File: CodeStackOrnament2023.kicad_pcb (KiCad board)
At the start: 2 copper layers, 70 x 70 mm, 28 parts, among them SW1 SW_SPST, U1 TLC555xD, U2 74VHC4040FT

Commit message: silkscreen logos
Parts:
- added G***: LOGO, LOGO, B.Cu at (131.8, 121.6)
- added G***: LOGO, LOGO, B.Cu at (173.7, 103.7)
- added G***: LOGO, LOGO, B.Cu at (129.1, 103.0)

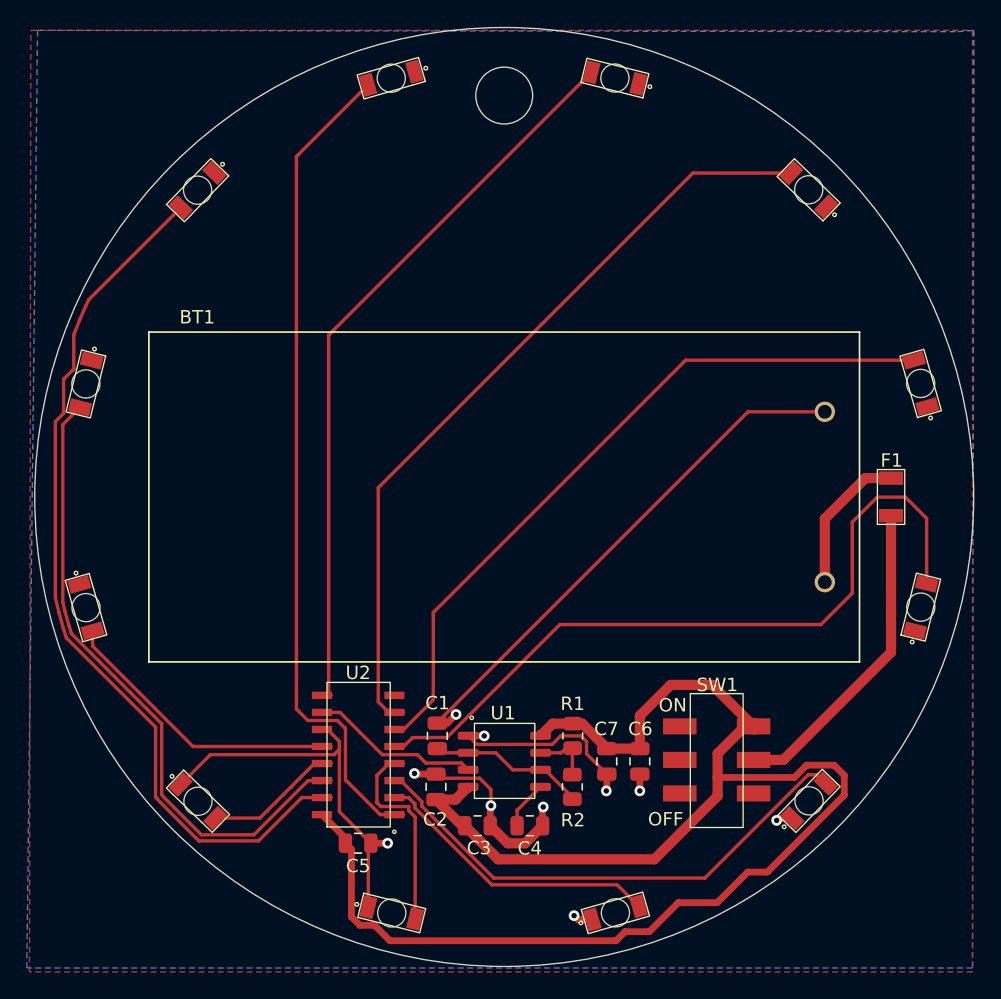
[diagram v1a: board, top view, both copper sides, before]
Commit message: adding qr code and a few more logos for silkscreen.
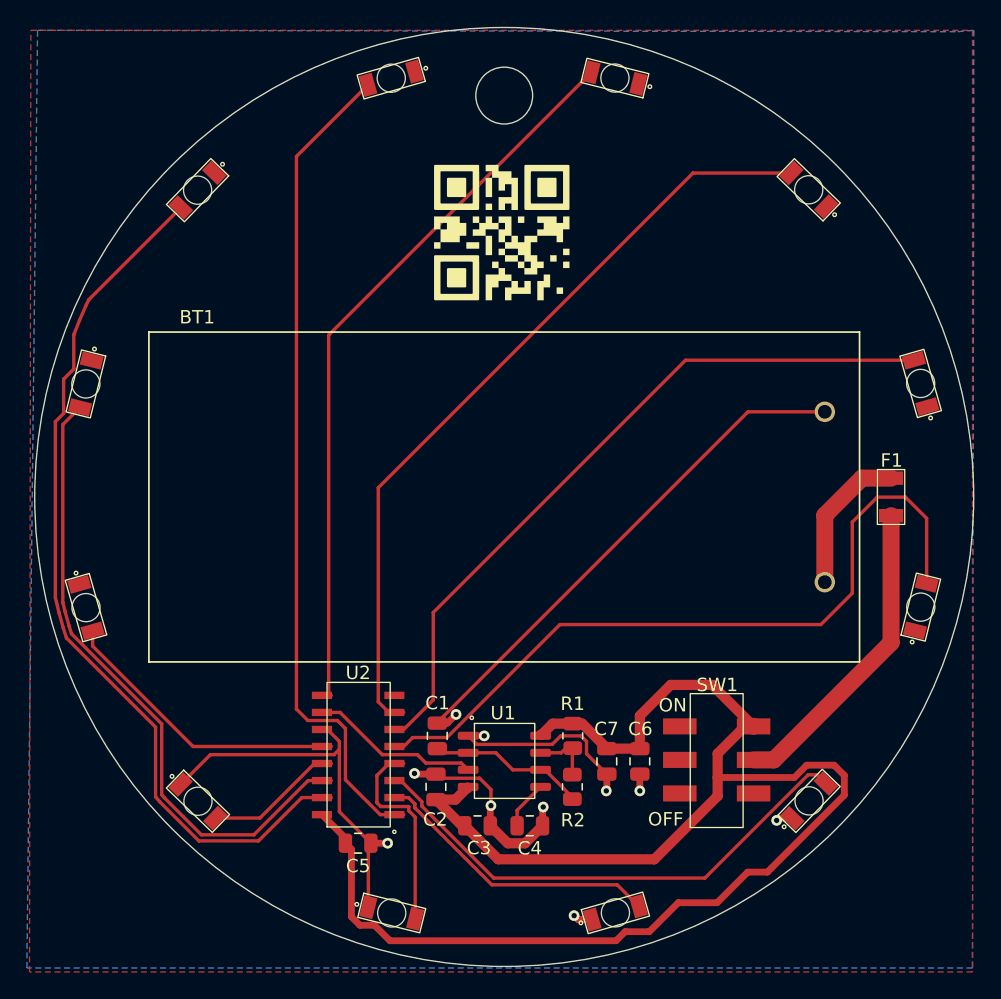
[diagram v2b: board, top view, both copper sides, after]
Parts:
- added G***: LOGO, LOGO, F.Cu at (149.9, 85.0)
- added G***: LOGO, LOGO, B.Cu at (127.3, 90.4)
- added G***: LOGO, LOGO, B.Cu at (171.6, 89.7)
- added G***: LOGO, LOGO, B.Cu at (171.6, 120.7)
- moved G*** 4.54 mm to (124.8, 104.5)
- moved G*** 2.16 mm to (150.1, 82.0)
- moved G*** 1.59 mm to (175.3, 103.7)
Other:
- board text added: "[1024]"
- board text added: "[128]"
- board text added: "[16]"
- board text added: "[1]"
- board text added: "[2048]"
- board text added: "[256]"
- board text added: "[2]"
- board text added: "[32]"
- board text added: "[4]"
- board text added: "[512]"
- board text added: "[64]"
- board text added: "[8]"

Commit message: fixing drc
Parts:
- moved G*** 0.55 mm to (149.8, 85.5)
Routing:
- net GND: track 103.8 -> 65.3 mm
- net Net-(D11-A): track 66.3 -> 66.9 mm
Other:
- board text added: "FROM: JON"
- board text added: "MERRY CHRISTMAS!"
- board text added: "SCAN FOR INSTRUCTIONS ->"
- board text added: "TO: ______________"

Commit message: fixing last drc
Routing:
- net GND: track 65.3 -> 20.1 mm

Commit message: aligning silkscreen
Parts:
- moved G*** 30.3 mm to (126.8, 91.8)
- moved G*** 27.2 mm to (126.8, 117.5)
- moved G*** 3.47 mm to (173.0, 117.5)
- moved G*** 2.46 mm to (173.0, 91.8)
- moved G*** 1.12 mm to (175.8, 104.7)
- moved G*** 0.78 mm to (150.2, 82.8)
- moved G*** 0.52 mm to (124.3, 104.7)
- moved G*** 0.17 mm to (150.2, 126.7)

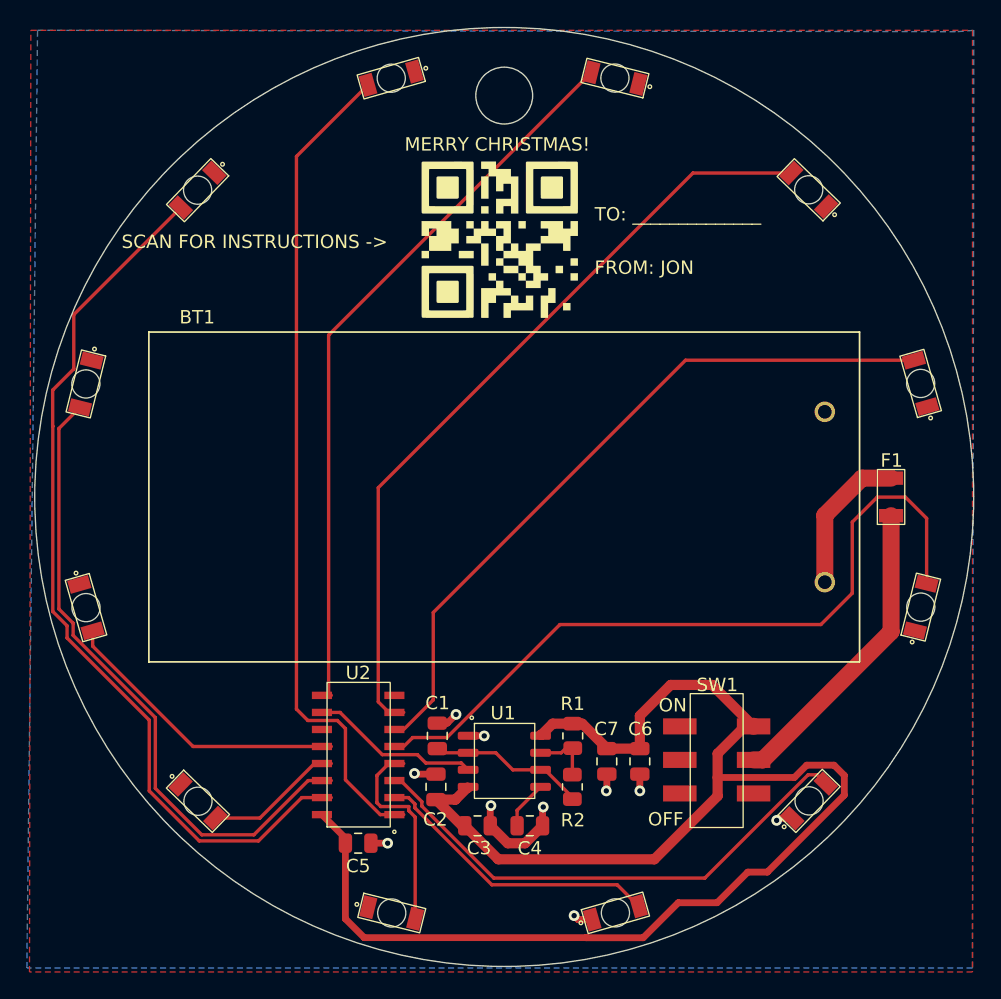
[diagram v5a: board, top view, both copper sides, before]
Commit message: more alignment with u2
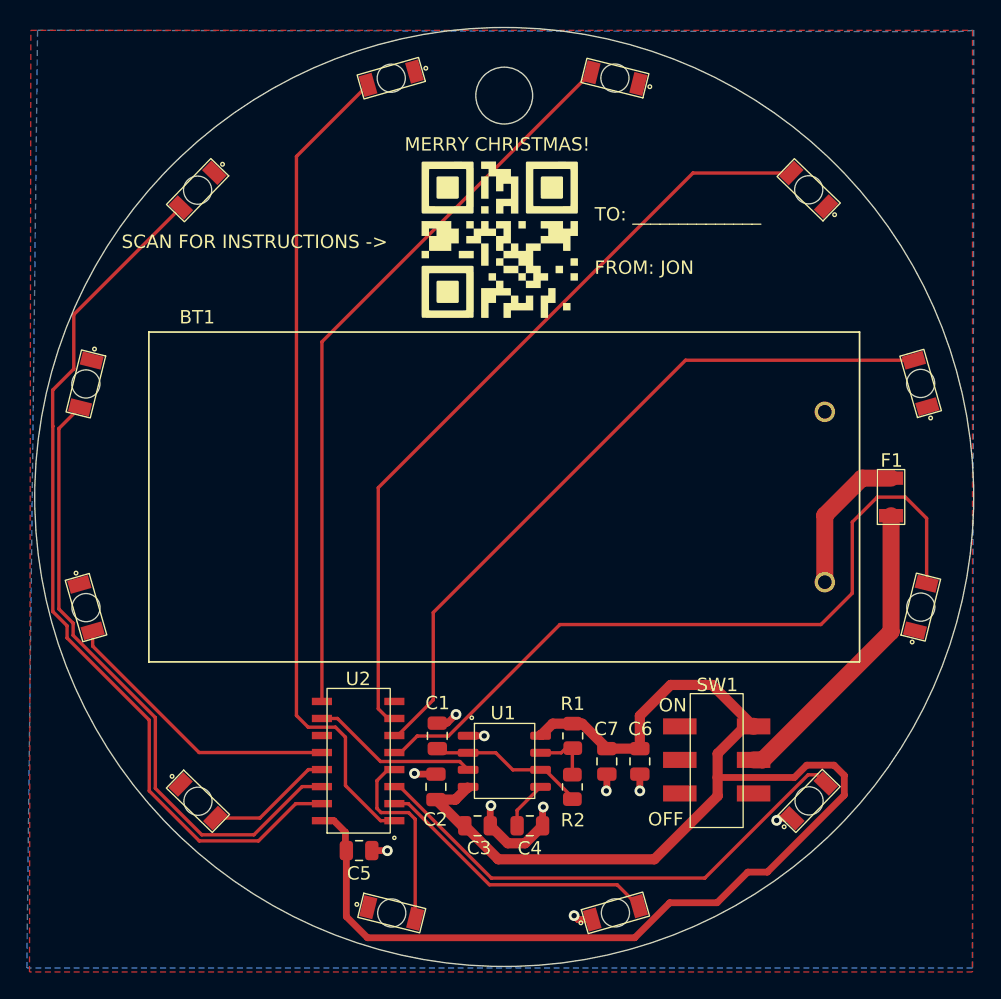
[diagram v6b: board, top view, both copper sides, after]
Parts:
- moved C5 0.55 mm to (139.3, 131.1)
- moved U2 0.45 mm to (141.9, 128.8)
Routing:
- net Net-(D7-A): track 15.5 -> 14.3 mm
- net Net-(D10-A): track 48.3 -> 47.4 mm
- net Net-(D3-A): track 53.3 -> 54.1 mm
- net Net-(D4-A): track 55.3 -> 56.2 mm
- net Net-(D8-A): track 10.3 -> 9.44 mm
- net Net-(D11-A): track 66.9 -> 66.0 mm
- net GND: track 20.1 -> 19.3 mm
- net Net-(D1-A): track 54.7 -> 55.2 mm
- net Net-(D9-A): track 22.0 -> 21.5 mm
- net Net-(U1-Q): track 12.0 -> 12.5 mm

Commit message: adding gerbers
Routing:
- net Net-(D2-A): track 58.5 -> 54.2 mm
- net Net-(D3-A): track 54.1 -> 50.3 mm
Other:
- board text added: "JLCJLCJLCJLC"
- board text added: "SCAN FOR DETAILS ->"
- board text removed: "SCAN FOR INSTRUCTIONS ->"
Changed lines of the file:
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@@
     (effects (font (size 1 1) (thickness 0.15)) (justify left bottom))
   )
-  (gr_text "SCAN FOR INSTRUCTIONS ->" (at 121.56 86.25) (layer "F.SilkS")
+  (gr_text "JLCJLCJLCJLC" (at 145.32 105.34) (layer "F.SilkS")
+    (effects (font (size 1 1) (thickness 0.15)) (justify left bottom))
+  )
+  (gr_text "SCAN FOR DETAILS ->" (at 125.78 86.32) (layer "F.SilkS")
     (effects (font (size 1 1) (thickness 0.15)) (justify left bottom))
   )
@@
   (segment (start 152.8 126.3) (end 151.05 128.05) (width 0.254) (layer "F.Cu") (net 5))
   (segment (start 151.05 128.05) (end 151.05 129.2) (width 0.254) (layer "F.Cu") (net 5))
-  (segment (start 136.5 119.931152) (end 136.5 93.119964) (width 0.254) (layer "F.Cu") (net 6))
-  (segment (start 136.5 93.119964) (end 156.596492 73.023472) (width 0.254) (layer "F.Cu") (net 6))
+  (segment (start 156.596492 73.193508) (end 156.596492 73.023472) (width 0.254) (layer "F.Cu") (net 6))
+  (segment (start 136.5 119.931152) (end 136.5 93.29) (width 0.254) (layer "F.Cu") (net 6))
+  (segment (start 136.5 93.29) (end 156.596492 73.193508) (width 0.254) (layer "F.Cu") (net 6))
+  (segment (start 171.482449 80.537551) (end 140.7 111.32) (width 0.254) (layer "F.Cu") (net 7))
+  (segment (start 140.7 111.32) (end 140.7 120.476152) (width 0.254) (layer "F.Cu") (net 7))
   (segment (start 140.7 120.476152) (end 141.425 121.201152) (width 0.254) (layer "F.Cu") (net 7))
-  (segment (start 140.7 104) (end 140.7 120.476152) (width 0.254) (layer "F.Cu") (net 7))
-  (segment (start 171.494652 80.537551) (end 164.162449 80.537551) (width 0.254) (layer "F.Cu") (net 7))
   (segment (start 141.425 121.201152) (end 141.9 121.201152) (width 0.254) (layer "F.Cu") (net 7))
-  (segment (start 164.162449 80.537551) (end 140.7 104) (width 0.254) (layer "F.Cu") (net 7))
-  (segment (start 144.8 119.82) (end 142.148848 122.471152) (width 0.254) (layer "F.Cu") (net 8))
-  (segment (start 142.148848 122.471152) (end 141.9 122.471152) (width 0.254) (layer "F.Cu") (net 8))
-  (segment (start 144.8 119.82) (end 144.8 113.3) (width 0.254) (layer "F.Cu") (net 8))
-  (segment (start 144.8 113.3) (end 163.605984 94.494016) (width 0.254) (layer "F.Cu") (net 8))
-  (segment (start 163.605984 94.494016) (end 180.6398 94.494016) (width 0.254) (layer "F.Cu") (net 8))
+  (segment (start 171.494652 80.537551) (end 171.482449 80.537551) (width 0.254) (layer "F.Cu") (net 7))
+  (segment (start 141.9 122.471152) (end 142.478848 122.471152) (width 0.254) (layer "F.Cu") (net 8))
+  (segment (start 142.478848 122.471152) (end 170.455984 94.494016) (width 0.254) (layer "F.Cu") (net 8))
+  (segment (start 170.455984 94.494016) (end 180.6398 94.494016) (width 0.254) (layer "F.Cu") (net 8))
   (segment (start 176.038 106.562) (end 176.038 111.862) (width 0.254) (layer "F.Cu") (net 9))
   (segment (start 177.9 104.7) (end 176.038 106.562) (width 0.254) (layer "F.Cu") (net 9))
@@
   (segment (start 119.408419 115.808419) (end 127.341152 123.741152) (width 0.254) (layer "F.Cu") (net 14))
   (segment (start 119.408419 114.667703) (end 119.408419 115.808419) (width 0.254) (layer "F.Cu") (net 14))
-  (segment (start 131.426034 129.873966) (end 127.545282 129.873966) (width 0.254) (layer "F.Cu") (net 15))
+  (segment (start 116.9 113.157948) (end 116.9 99.5752) (width 0.254) (layer "F.Cu") (net 15))
+  (segment (start 124.08 121.134065) (end 118.174 115.228065) (width 0.254) (layer "F.Cu") (net 15))
+  (segment (start 116.9 99.5752) (end 118.466724 98.008476) (width 0.254) (layer "F.Cu") (net 15))
+  (segment (start 136.025 126.281152) (end 132.432186 129.873966) (width 0.254) (layer "F.Cu") (net 15))
   (segment (start 127.545282 129.873966) (end 124.08 126.408684) (width 0.254) (layer "F.Cu") (net 15))
-  (segment (start 135.018848 126.281152) (end 136.5 126.281152) (width 0.254) (layer "F.Cu") (net 15))
-  (segment (start 116.89 113.037948) (end 116.89 99.5852) (width 0.254) (layer "F.Cu") (net 15))
-  (segment (start 124.08 121.134064) (end 117.954 115.008064) (width 0.254) (layer "F.Cu") (net 15))
-  (segment (start 117.954 115.008064) (end 117.954 114.101948) (width 0.254) (layer "F.Cu") (net 15))
-  (segment (start 117.954 114.101948) (end 116.89 113.037948) (width 0.254) (layer "F.Cu") (net 15))
-  (segment (start 116.89 99.5852) (end 118.466724 98.008476) (width 0.254) (layer "F.Cu") (net 15))
-  (segment (start 124.08 126.408684) (end 124.08 121.134064) (width 0.254) (layer "F.Cu") (net 15))
-  (segment (start 131.426034 129.873966) (end 135.018848 126.281152) (width 0.254) (layer "F.Cu") (net 15))
-  (segment (start 117.5 114.29) (end 116.436 113.226) (width 0.254) (layer "F.Cu") (net 16))
-  (segment (start 123.626 126.596736) (end 123.626 121.322116) (width 0.254) (layer "F.Cu") (net 16))
-  (segment (start 116.426 96.720044) (end 118 95.146044) (width 0.254) (layer "F.Cu") (net 16))
-  (segment (start 116.436 99.417147) (end 116.426 99.407147) (width 0.254) (layer "F.Cu") (net 16))
-  (segment (start 117.5 115.196116) (end 117.5 114.29) (width 0.254) (layer "F.Cu") (net 16))
-  (segment (start 131.772034 130.327966) (end 134.548848 127.551152) (width 0.254) (layer "F.Cu") (net 16))
-  (segment (start 118 91.091119) (end 125.980803 83.110316) (width 0.254) (layer "F.Cu") (net 16))
-  (segment (start 131.772034 130.327966) (end 127.35723 130.327966) (width 0.254) (layer "F.Cu") (net 16))
-  (segment (start 118 95.146044) (end 118 91.091119) (width 0.254) (layer "F.Cu") (net 16))
-  (segment (start 116.426 99.407147) (end 116.426 96.720044) (width 0.254) (layer "F.Cu") (net 16))
+  (segment (start 118.174 115.228065) (end 118.174 114.431948) (width 0.254) (layer "F.Cu") (net 15))
+  (segment (start 124.08 126.408684) (end 124.08 121.134065) (width 0.254) (layer "F.Cu") (net 15))
+  (segment (start 118.174 114.431948) (end 116.9 113.157948) (width 0.254) (layer "F.Cu") (net 15))
+  (segment (start 136.5 126.281152) (end 136.025 126.281152) (width 0.254) (layer "F.Cu") (net 15))
+  (segment (start 132.432186 129.873966) (end 127.545282 129.873966) (width 0.254) (layer "F.Cu") (net 15))
+  (segment (start 117.31 94.5) (end 125.980803 85.829197) (width 0.254) (layer "F.Cu") (net 16))
+  (segment (start 133.248186 130.327966) (end 127.35723 130.327966) (width 0.254) (layer "F.Cu") (net 16))
+  (segment (start 116.446 113.346) (end 116.446 97.204) (width 0.254) (layer "F.Cu") (net 16))
+  (segment (start 136.025 127.551152) (end 133.248186 130.327966) (width 0.254) (layer "F.Cu") (net 16))
+  (segment (start 125.980803 85.829197) (end 125.980803 83.110316) (width 0.254) (layer "F.Cu") (net 16))
+  (segment (start 117.31 96.34) (end 117.31 94.5) (width 0.254) (layer "F.Cu") (net 16))
+  (segment (start 117.72 114.62) (end 116.446 113.346) (width 0.254) (layer "F.Cu") (net 16))
+  (segment (start 117.72 115.416117) (end 117.72 114.62) (width 0.254) (layer "F.Cu") (net 16))
   (segment (start 127.35723 130.327966) (end 123.626 126.596736) (width 0.254) (layer "F.Cu") (net 16))
-  (segment (start 134.548848 127.551152) (end 136.5 127.551152) (width 0.254) (layer "F.Cu") (net 16))
-  (segment (start 116.436 113.226) (end 116.436 99.417147) (width 0.254) (layer "F.Cu") (net 16))
-  (segment (start 123.626 121.322116) (end 117.5 115.196116) (width 0.254) (layer "F.Cu") (net 16))
-  (segment (start 137.51 121.85) (end 138.254 122.594) (width 0.254) (layer "F.Cu") (net 17))
+  (segment (start 136.5 127.551152) (end 136.025 127.551152) (width 0.254) (layer "F.Cu") (net 16))
+  (segment (start 123.626 121.322117) (end 117.72 115.416117) (width 0.254) (layer "F.Cu") (net 16))
+  (segment (start 116.446 97.204) (end 117.31 96.34) (width 0.254) (layer "F.Cu") (net 16))
+  (segment (start 123.626 126.596736) (end 123.626 121.322117) (width 0.254) (layer "F.Cu") (net 16))
+  (segment (start 139.937266 73.965171) (end 134.6 79.302437) (width 0.254) (layer "F.Cu") (net 17))
   (segment (start 134.6 79.302437) (end 134.6 120.980152) (width 0.254) (layer "F.Cu") (net 17))
+  (segment (start 140.05 128) (end 140.871152 128.821152) (width 0.254) (layer "F.Cu") (net 17))
   (segment (start 135.469848 121.85) (end 137.51 121.85) (width 0.254) (layer "F.Cu") (net 17))
-  (segment (start 139.937266 73.965171) (end 134.6 79.302437) (width 0.254) (layer "F.Cu") (net 17))
-  (segment (start 138.254 122.594) (end 138.254 126.204) (width 0.254) (layer "F.Cu") (net 17))
-  (segment (start 138.254 126.204) (end 140.871152 128.821152) (width 0.254) (layer "F.Cu") (net 17))
+  (segment (start 137.51 121.85) (end 140.05 124.39) (width 0.254) (layer "F.Cu") (net 17))
   (segment (start 140.871152 128.821152) (end 141.9 128.821152) (width 0.254) (layer "F.Cu") (net 17))
   (segment (start 134.6 120.980152) (end 135.469848 121.85) (width 0.254) (layer "F.Cu") (net 17))
+  (segment (start 140.05 124.39) (end 140.05 128) (width 0.254) (layer "F.Cu") (net 17))
   (segment (start 154.6875 123.4125) (end 154.34 123.76) (width 0.254) (layer "F.Cu") (net 18))
   (segment (start 155.2 123.4125) (end 154.6875 123.4125) (width 0.254) (layer "F.Cu") (net 18))

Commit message: adding gerbers. cleaning up schematic.
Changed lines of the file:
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@@
       (plotinvisibletext false)
       (sketchpadsonfab false)
-      (subtractmaskfromsilk false)
+      (subtractmaskfromsilk true)
       (outputformat 1)
       (mirror false)
-      (drillshape 1)
+      (drillshape 0)
       (scaleselection 1)
-      (outputdirectory "")
+      (outputdirectory "Gerbers/")
     )
   )
@@
     (fp_line (start 1 0.625) (end -1 0.625)
       (stroke (width 0.1) (type solid)) (layer "F.Fab"))
-    (pad "1" smd roundrect (at -0.9125 0 270) (size 1.025 1.4) (layers "F.Cu" "F.Paste" "F.Mask") (roundrect_rratio 0.243902)
+    (pad "1" smd roundrect (at -0.9125 0 270) (size 1.025 1.4) (layers "F.Cu" "F.Paste" "F.Mask") (roundrect_rratio 0.243902439)
       (net 18 "Net-(U1-DIS)") (pintype "passive"))
-    (pad "2" smd roundrect (at 0.9125 0 270) (size 1.025 1.4) (layers "F.Cu" "F.Paste" "F.Mask") (roundrect_rratio 0.243902)
+    (pad "2" smd roundrect (at 0.9125 0 270) (size 1.025 1.4) (layers "F.Cu" "F.Paste" "F.Mask") (roundrect_rratio 0.243902439)
       (net 3 "Net-(U1-THR)") (pintype "passive"))
     (model "${KICAD6_3DMODEL_DIR}/Resistor_SMD.3dshapes/R_0805_2012Metric.wrl"
@@
     (fp_line (start 1 0.625) (end -1 0.625)
       (stroke (width 0.1) (type solid)) (layer "F.Fab"))
-    (pad "1" smd roundrect (at -0.9125 0 270) (size 1.025 1.4) (layers "F.Cu" "F.Paste" "F.Mask") (roundrect_rratio 0.243902)
+    (pad "1" smd roundrect (at -0.9125 0 270) (size 1.025 1.4) (layers "F.Cu" "F.Paste" "F.Mask") (roundrect_rratio 0.243902439)
       (net 4 "+3V0") (pintype "passive"))
-    (pad "2" smd roundrect (at 0.9125 0 270) (size 1.025 1.4) (layers "F.Cu" "F.Paste" "F.Mask") (roundrect_rratio 0.243902)
+    (pad "2" smd roundrect (at 0.9125 0 270) (size 1.025 1.4) (layers "F.Cu" "F.Paste" "F.Mask") (roundrect_rratio 0.243902439)
       (net 18 "Net-(U1-DIS)") (pintype "passive"))
     (model "${KICAD6_3DMODEL_DIR}/Resistor_SMD.3dshapes/R_0805_2012Metric.wrl"
